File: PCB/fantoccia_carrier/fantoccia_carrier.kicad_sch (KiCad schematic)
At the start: 4 parts, among them J2 1881545, J3 1881545, J4 1881545, J5 1881545

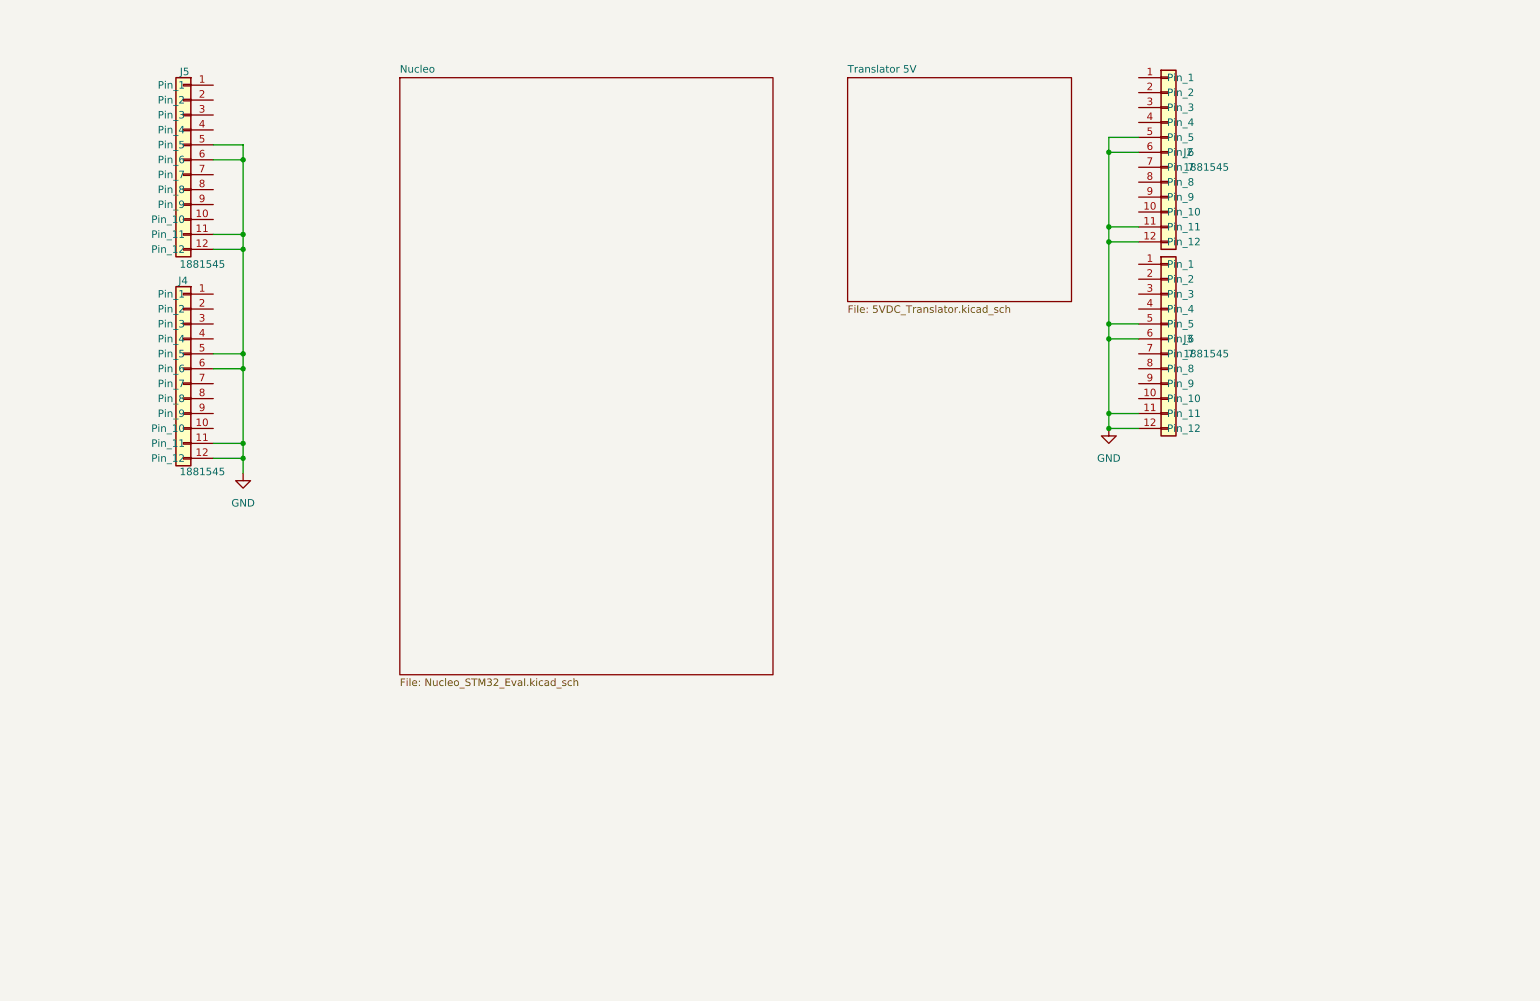
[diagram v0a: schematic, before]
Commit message: PCB Created
Schematic mostly finished, just need to figure out pinning and add more TVS protection. Created PCB might need to tweak footprint.
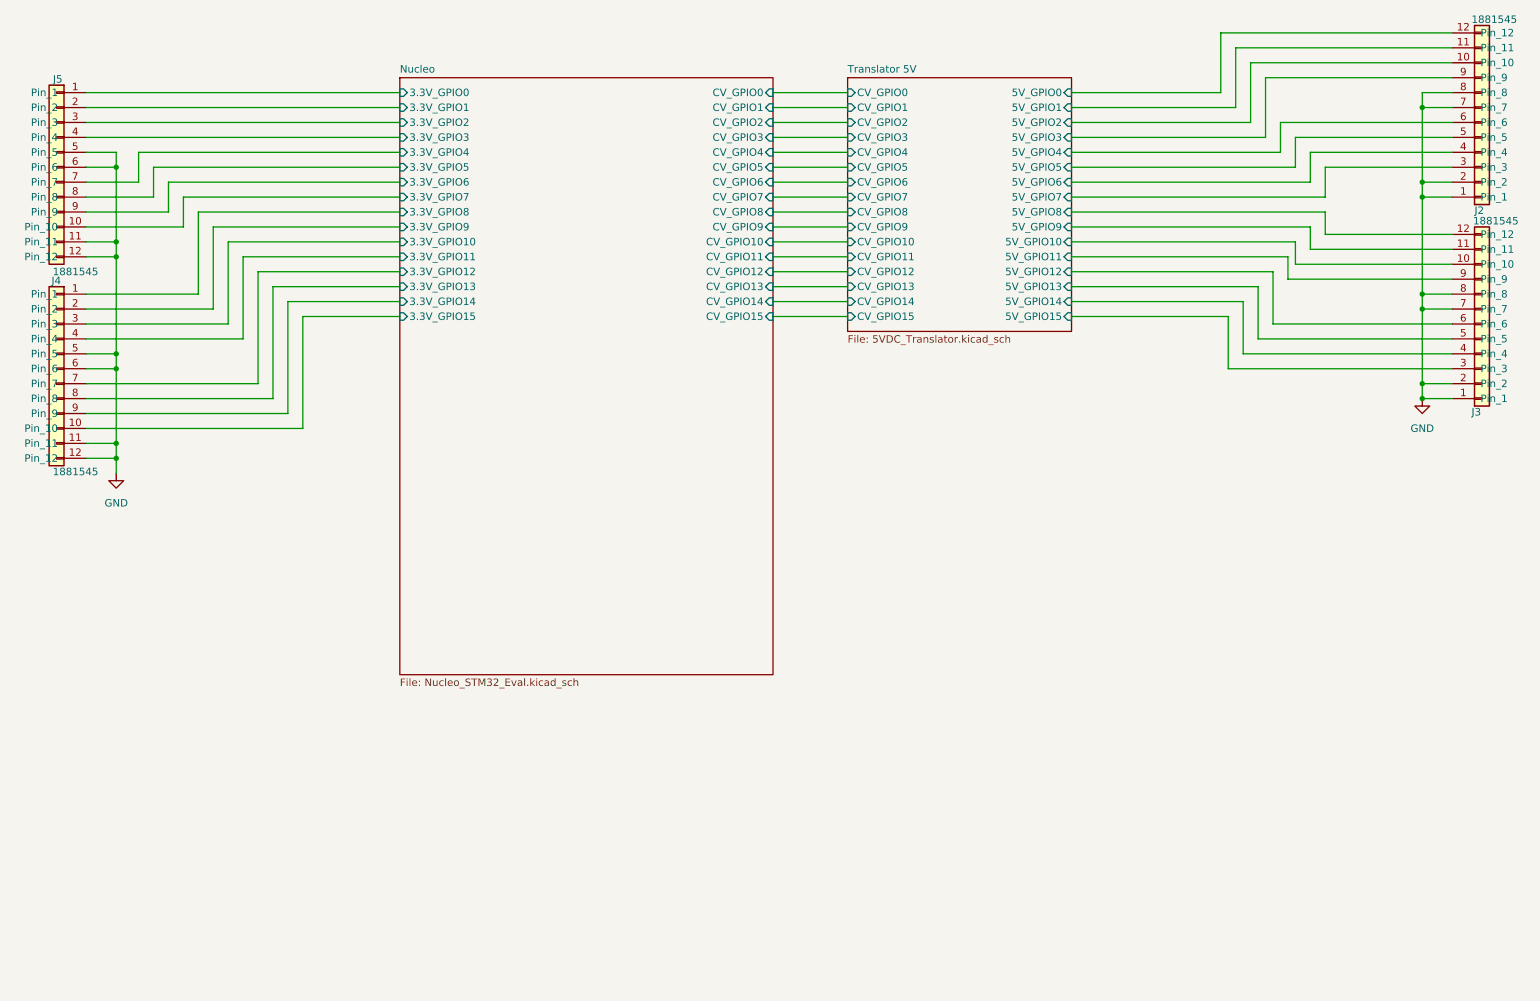
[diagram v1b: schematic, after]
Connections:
- net GND: now also J2.1 (Pin_1), J2.2 (Pin_2), J2.7 (Pin_7), J2.8 (Pin_8), J3.1 (Pin_1), J3.2 (Pin_2), J3.7 (Pin_7), J3.8 (Pin_8); no longer J2.11 (Pin_11), J2.12 (Pin_12), J2.5 (Pin_5), J2.6 (Pin_6), J3.11 (Pin_11), J3.12 (Pin_12), J3.5 (Pin_5), J3.6 (Pin_6)
- net Nucleo/3.3V_GPIO8: now reaches J4.1 (Pin_1)
- net Nucleo/3.3V_GPIO15: now reaches J4.10 (Pin_10)
- net Nucleo/3.3V_GPIO9: now reaches J4.2 (Pin_2)
- net Nucleo/3.3V_GPIO10: now reaches J4.3 (Pin_3)
- net Nucleo/3.3V_GPIO11: now reaches J4.4 (Pin_4)
- net Nucleo/3.3V_GPIO12: now reaches J4.7 (Pin_7)
- net Nucleo/3.3V_GPIO13: now reaches J4.8 (Pin_8)
- net Nucleo/3.3V_GPIO14: now reaches J4.9 (Pin_9)
- net Nucleo/3.3V_GPIO0: now reaches J5.1 (Pin_1)
- net Nucleo/3.3V_GPIO7: now reaches J5.10 (Pin_10)
- net Nucleo/3.3V_GPIO1: now reaches J5.2 (Pin_2)
- net Nucleo/3.3V_GPIO2: now reaches J5.3 (Pin_3)
- net Nucleo/3.3V_GPIO3: now reaches J5.4 (Pin_4)
- net Nucleo/3.3V_GPIO4: now reaches J5.7 (Pin_7)
- net Nucleo/3.3V_GPIO5: now reaches J5.8 (Pin_8)
- net Nucleo/3.3V_GPIO6: now reaches J5.9 (Pin_9)
- net Translator 5V/5V_GPIO2: now reaches J2.10 (Pin_10)
- net Translator 5V/5V_GPIO7: now reaches J2.3 (Pin_3)
- net Translator 5V/5V_GPIO6: now reaches J2.4 (Pin_4)
- net Translator 5V/5V_GPIO3: now reaches J2.9 (Pin_9)
- net Translator 5V/5V_GPIO10: now reaches J3.10 (Pin_10)
- net Translator 5V/5V_GPIO15: now reaches J3.3 (Pin_3)
- net Translator 5V/5V_GPIO14: now reaches J3.4 (Pin_4)
- net Translator 5V/5V_GPIO11: now reaches J3.9 (Pin_9)
- new net Translator 5V/5V_GPIO0: J2.12 (Pin_12)
- new net Translator 5V/5V_GPIO1: J2.11 (Pin_11)
- new net Translator 5V/5V_GPIO12: J3.6 (Pin_6)
- new net Translator 5V/5V_GPIO13: J3.5 (Pin_5)
- new net Translator 5V/5V_GPIO4: J2.6 (Pin_6)
- new net Translator 5V/5V_GPIO5: J2.5 (Pin_5)
- new net Translator 5V/5V_GPIO8: J3.12 (Pin_12)
- new net Translator 5V/5V_GPIO9: J3.11 (Pin_11)
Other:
- sheet Nucleo ports: added 3.3V_GPIO0, 3.3V_GPIO1, 3.3V_GPIO10, 3.3V_GPIO11, 3.3V_GPIO12, 3.3V_GPIO13, 3.3V_GPIO14, 3.3V_GPIO15, 3.3V_GPIO2, 3.3V_GPIO3, 3.3V_GPIO4, 3.3V_GPIO5, 3.3V_GPIO6, 3.3V_GPIO7, 3.3V_GPIO8, 3.3V_GPIO9, CV_GPIO0, CV_GPIO1, CV_GPIO10, CV_GPIO11, CV_GPIO12, CV_GPIO13, CV_GPIO14, CV_GPIO15, CV_GPIO2, CV_GPIO3, CV_GPIO4, CV_GPIO5, CV_GPIO6, CV_GPIO7, CV_GPIO8, CV_GPIO9; removed none
- sheet Translator 5V ports: added 5V_GPIO0, 5V_GPIO1, 5V_GPIO10, 5V_GPIO11, 5V_GPIO12, 5V_GPIO13, 5V_GPIO14, 5V_GPIO15, 5V_GPIO2, 5V_GPIO3, 5V_GPIO4, 5V_GPIO5, 5V_GPIO6, 5V_GPIO7, 5V_GPIO8, 5V_GPIO9, CV_GPIO0, CV_GPIO1, CV_GPIO10, CV_GPIO11, CV_GPIO12, CV_GPIO13, CV_GPIO14, CV_GPIO15, CV_GPIO2, CV_GPIO3, CV_GPIO4, CV_GPIO5, CV_GPIO6, CV_GPIO7, CV_GPIO8, CV_GPIO9; removed none
- moved on the sheet: J2, J3, J4, J5

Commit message: PCB progress and feature updates
Added another bank of 5V channels. PCB layout figured out, board shape defined. 3D model added to STM32 evaluation kit. Now just need to determine pinout and add protection circuitry to pins.
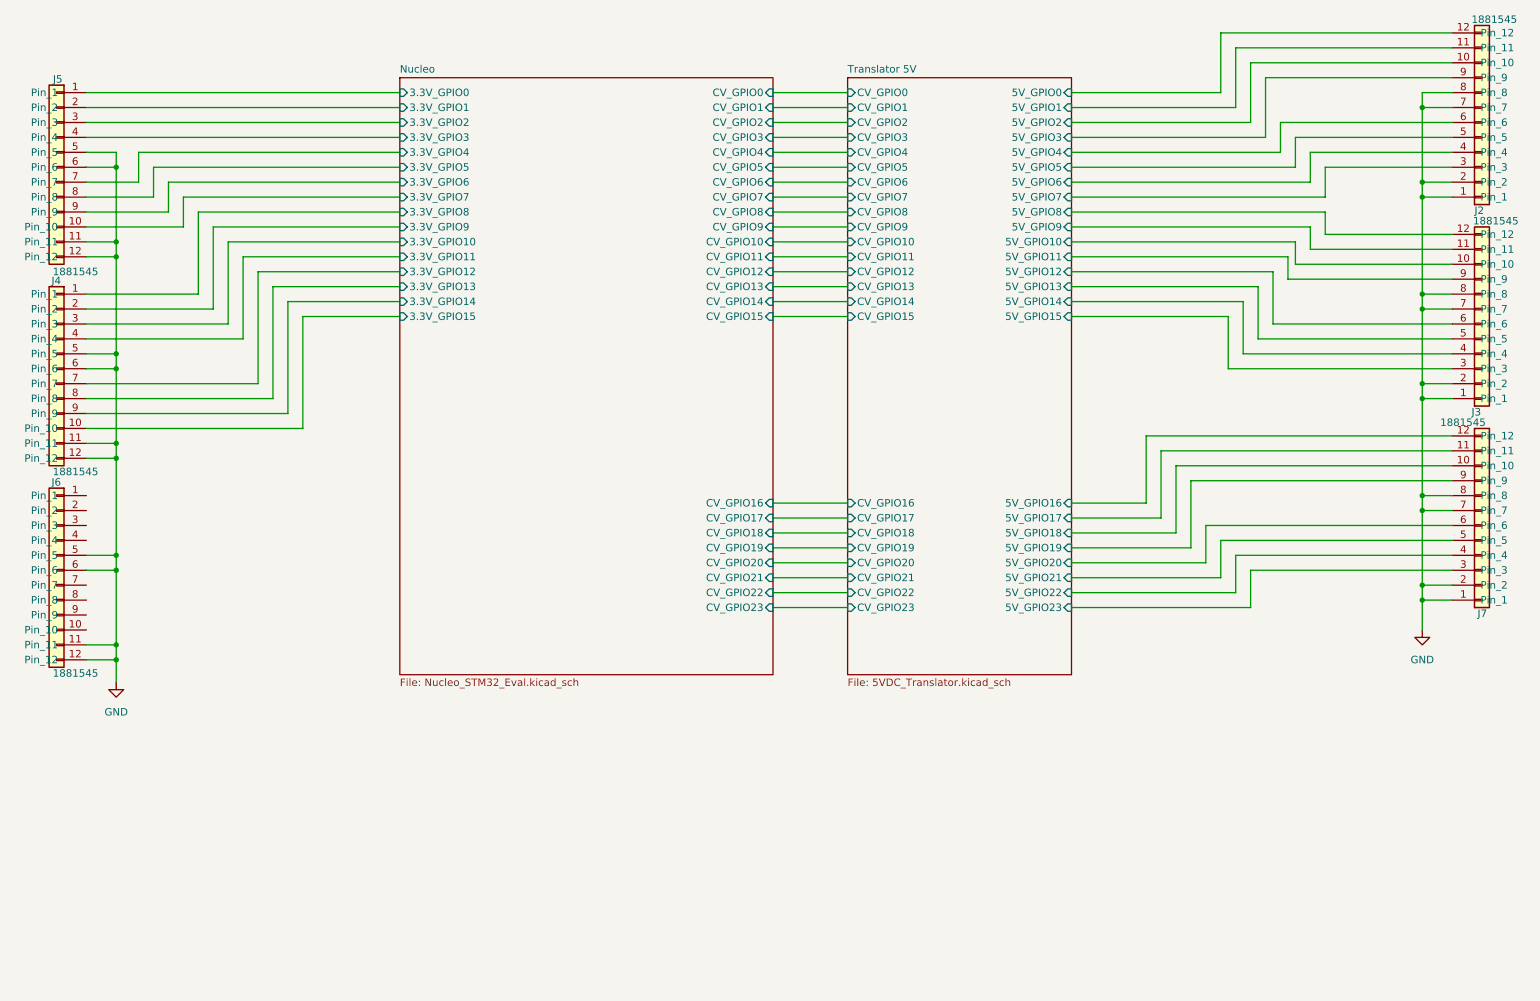
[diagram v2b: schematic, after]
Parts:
- added J6, J7: 1881545, AVR-KiCAD-Lib-Connectors:PHOENIX_1881545, symbol AVR-KiCAD-Lib-Connectors:1881545
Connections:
- net GND: now also J6.11 (Pin_11), J6.12 (Pin_12), J6.5 (Pin_5), J6.6 (Pin_6), J7.1 (Pin_1), J7.2 (Pin_2), J7.7 (Pin_7), J7.8 (Pin_8)
- new net Translator 5V/5V_GPIO16: J7.12 (Pin_12)
- new net Translator 5V/5V_GPIO17: J7.11 (Pin_11)
- new net Translator 5V/5V_GPIO18: J7.10 (Pin_10)
- new net Translator 5V/5V_GPIO19: J7.9 (Pin_9)
- new net Translator 5V/5V_GPIO20: J7.6 (Pin_6)
- new net Translator 5V/5V_GPIO21: J7.5 (Pin_5)
- new net Translator 5V/5V_GPIO22: J7.4 (Pin_4)
- new net Translator 5V/5V_GPIO23: J7.3 (Pin_3)
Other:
- sheet Nucleo ports: added CV_GPIO16, CV_GPIO17, CV_GPIO18, CV_GPIO19, CV_GPIO20, CV_GPIO21, CV_GPIO22, CV_GPIO23; removed none
- sheet Translator 5V ports: added 5V_GPIO16, 5V_GPIO17, 5V_GPIO18, 5V_GPIO19, 5V_GPIO20, 5V_GPIO21, 5V_GPIO22, 5V_GPIO23, CV_GPIO16, CV_GPIO17, CV_GPIO18, CV_GPIO19, CV_GPIO20, CV_GPIO21, CV_GPIO22, CV_GPIO23; removed none

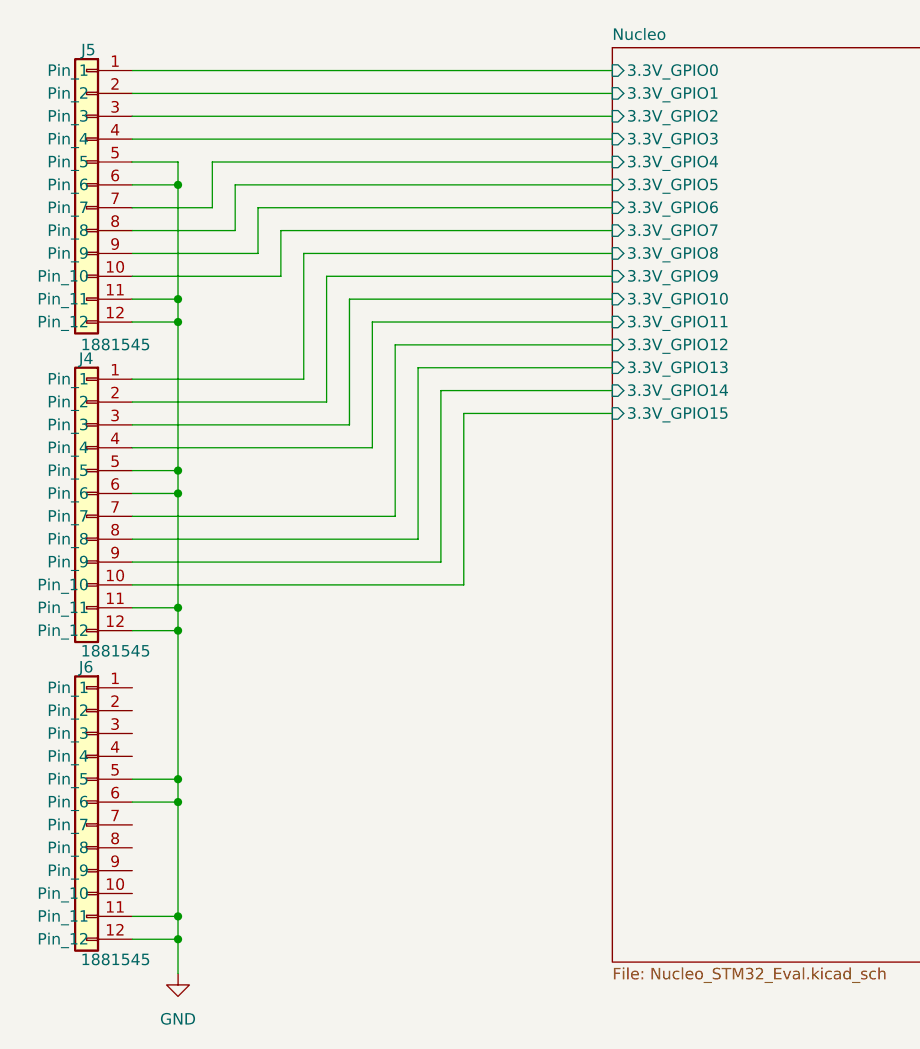
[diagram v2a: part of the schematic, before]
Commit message: Design Rules
Created Design rules, added more IO connections, need to figure out pinning next.
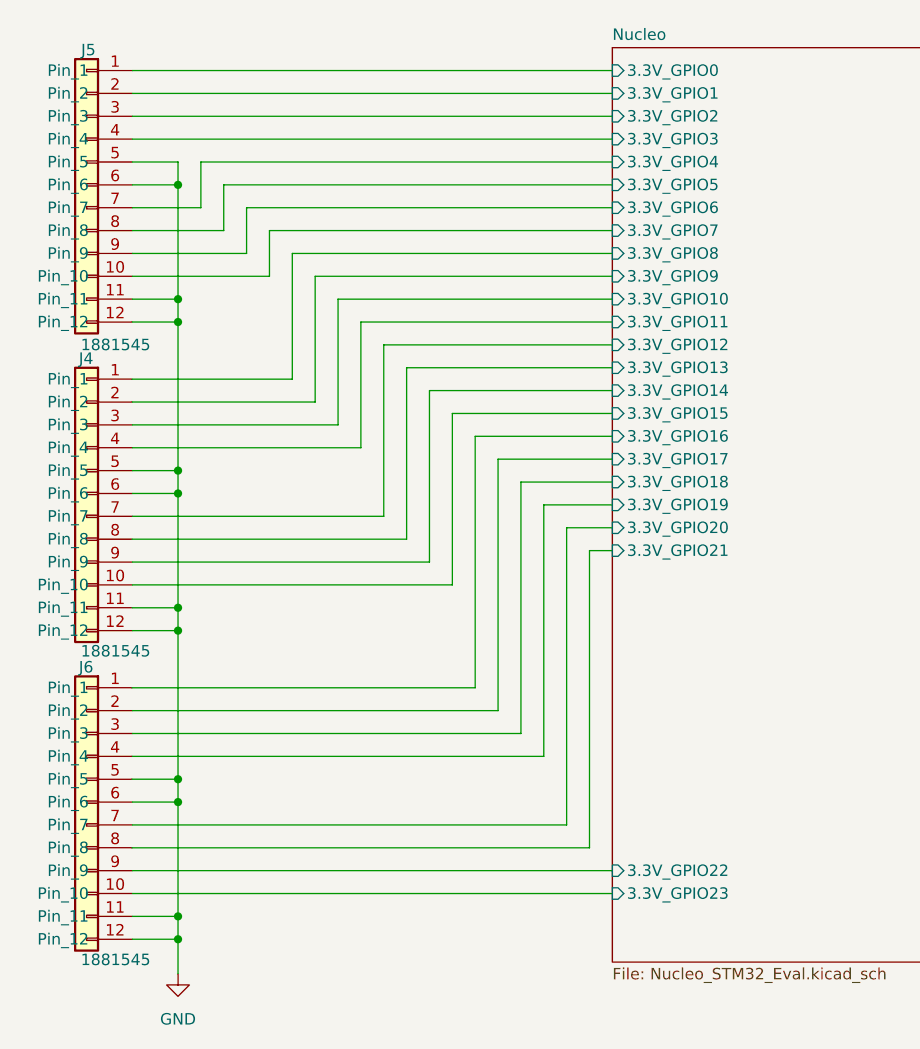
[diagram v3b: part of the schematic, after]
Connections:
- net Nucleo/3.3V_GPIO16: now reaches J6.1 (Pin_1)
- net Nucleo/3.3V_GPIO23: now reaches J6.10 (Pin_10)
- net Nucleo/3.3V_GPIO17: now reaches J6.2 (Pin_2)
- net Nucleo/3.3V_GPIO18: now reaches J6.3 (Pin_3)
- net Nucleo/3.3V_GPIO19: now reaches J6.4 (Pin_4)
- net Nucleo/3.3V_GPIO20: now reaches J6.7 (Pin_7)
- net Nucleo/3.3V_GPIO21: now reaches J6.8 (Pin_8)
- net Nucleo/3.3V_GPIO22: now reaches J6.9 (Pin_9)
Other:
- sheet Nucleo ports: added 3.3V_GPIO16, 3.3V_GPIO17, 3.3V_GPIO18, 3.3V_GPIO19, 3.3V_GPIO20, 3.3V_GPIO21, 3.3V_GPIO22, 3.3V_GPIO23; removed none

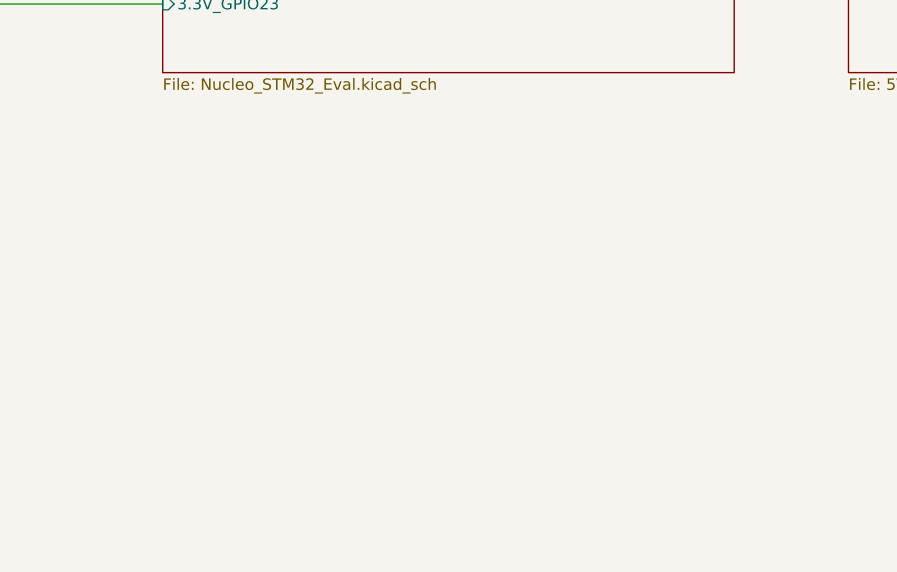
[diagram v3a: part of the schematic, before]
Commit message: PCB and Pinout
Progress made with PCB wiring eval board pins to pheonix connectors. Pinout almost completely chosen but subject to revision !
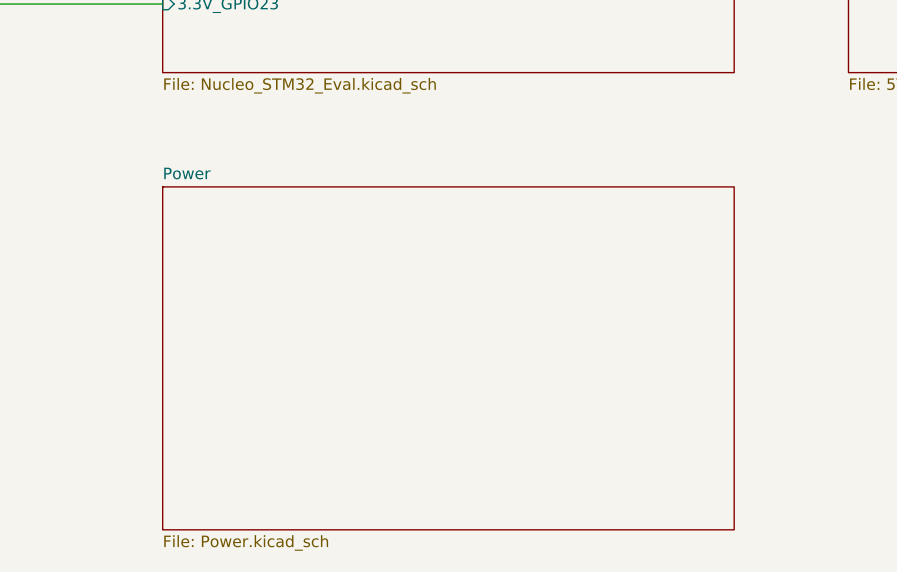
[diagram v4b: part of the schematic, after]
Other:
- added sheet Power (Power.kicad_sch)
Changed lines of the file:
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@@
+	)
+	(sheet
+		(at 88.9 152.4)
+		(size 63.5 38.1)
+		(fields_autoplaced yes)
+		(stroke
+			(width 0.1524)
+			(type solid)
+		)
+		(fill
+			(color 0 0 0 0.0000)
+		)
+		(property "Sheetname" "Power"
+			(at 88.9 151.6884 0)
+			(effects
+				(font
+					(size 1.27 1.27)
+				)
+				(justify left bottom)
+			)
+		)
+		(property "Sheetfile" "Power.kicad_sch"
+			(at 88.9 191.0846 0)
+			(effects
+				(font
+					(size 1.27 1.27)
+				)
+				(justify left top)
+			)
+		)
+		(instances
+			(project "fantoccia_carrier"
+				(path "/faa652bd-d277-4d95-a530-1d3e26469af1"
+					(page "4")
+				)
+			)
+		)
 	)
 	(sheet
